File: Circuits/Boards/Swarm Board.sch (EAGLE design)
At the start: 78 parts, among them CON1 ISP(2X3), T1 NPN2N2222, T10 TEFT4300, T11 NPN2N2222, T12 NPN2N2222, T2 NPN2N2222, T3 NPN2N2222, T4 TEFT4300, T5 TEFT4300, T6 TEFT4300, T7 TEFT4300, T8 TEFT4300, T9 TEFT4300, U1 ATMEGA324P, U2 MCP73832SOT-23, U3 TB6552FN/FNG

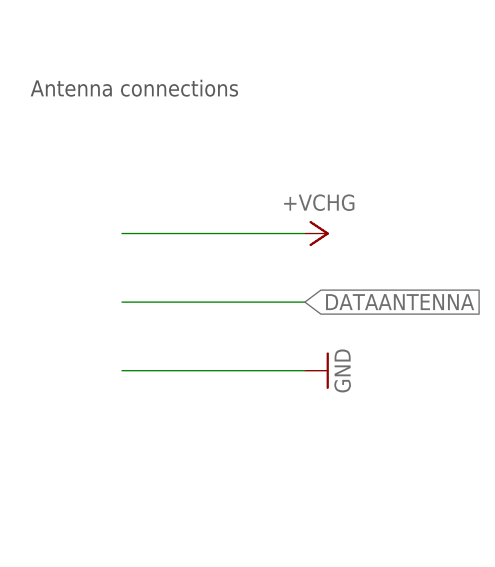
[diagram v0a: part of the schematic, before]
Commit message: 
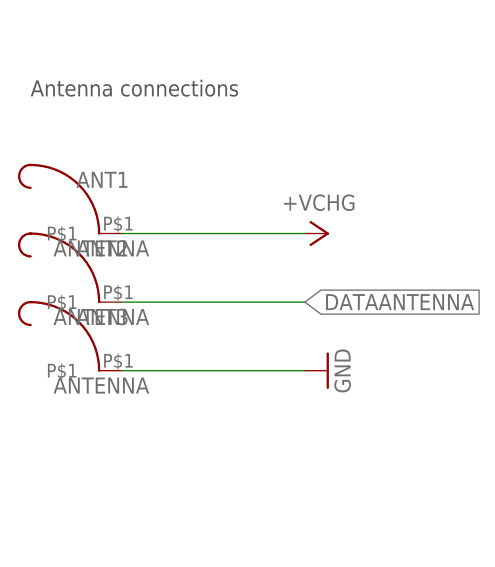
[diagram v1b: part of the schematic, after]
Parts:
- added ANT1, ANT2, ANT3: ANTENNA, Mechanical:ANTENNA
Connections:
- net +VCHG: now also ANT1.P$1
- net DATAANTENNA: now also ANT2.P$1
- net GND: now also ANT3.P$1
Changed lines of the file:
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@@
 <part name="C11" library="Passive" deviceset="CAP" device="0603" value="12pf"/>
 <part name="GND27" library="Supply" deviceset="GND" device=""/>
+<part name="ANT1" library="Mechanical" deviceset="ANTENNA" device=""/>
+<part name="ANT2" library="Mechanical" deviceset="ANTENNA" device=""/>
+<part name="ANT3" library="Mechanical" deviceset="ANTENNA" device=""/>
 </parts>
 <sheets>
@@
 <instance part="C11" gate="G$1" x="-45.72" y="-7.62" rot="R270"/>
 <instance part="GND27" gate="1" x="-55.88" y="-5.08" rot="R270"/>
+<instance part="ANT1" gate="G$1" x="-271.78" y="-48.26"/>
+<instance part="ANT2" gate="G$1" x="-271.78" y="-55.88"/>
+<instance part="ANT3" gate="G$1" x="-271.78" y="-63.5"/>
 </instances>
 <busses>
@@
 <pinref part="GND18" gate="1" pin="GND"/>
 <wire x1="-251.46" y1="-63.5" x2="-271.78" y2="-63.5" width="0.1524" layer="91"/>
+<pinref part="ANT3" gate="G$1" pin="P$1"/>
 </segment>
 <segment>
@@
 <pinref part="P+15" gate="G$1" pin="+VCHG"/>
 <wire x1="-251.46" y1="-48.26" x2="-271.78" y2="-48.26" width="0.1524" layer="91"/>
+<pinref part="ANT1" gate="G$1" pin="P$1"/>
 </segment>
 <segment>
@@
 <wire x1="-251.46" y1="-55.88" x2="-271.78" y2="-55.88" width="0.1524" layer="91"/>
 <label x="-251.46" y="-55.88" size="1.778" layer="91" xref="yes"/>
-</segment>
-</net>
+<pinref part="ANT2" gate="G$1" pin="P$1"/>
+</segment>
+</net>
